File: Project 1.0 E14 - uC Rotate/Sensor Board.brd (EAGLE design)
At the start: 40 x 75.1 mm, 98 parts, among them IC1 LT1963EST-1.5, IC2 LT1963EST-1.5, IC4 LT1963EST-1.5

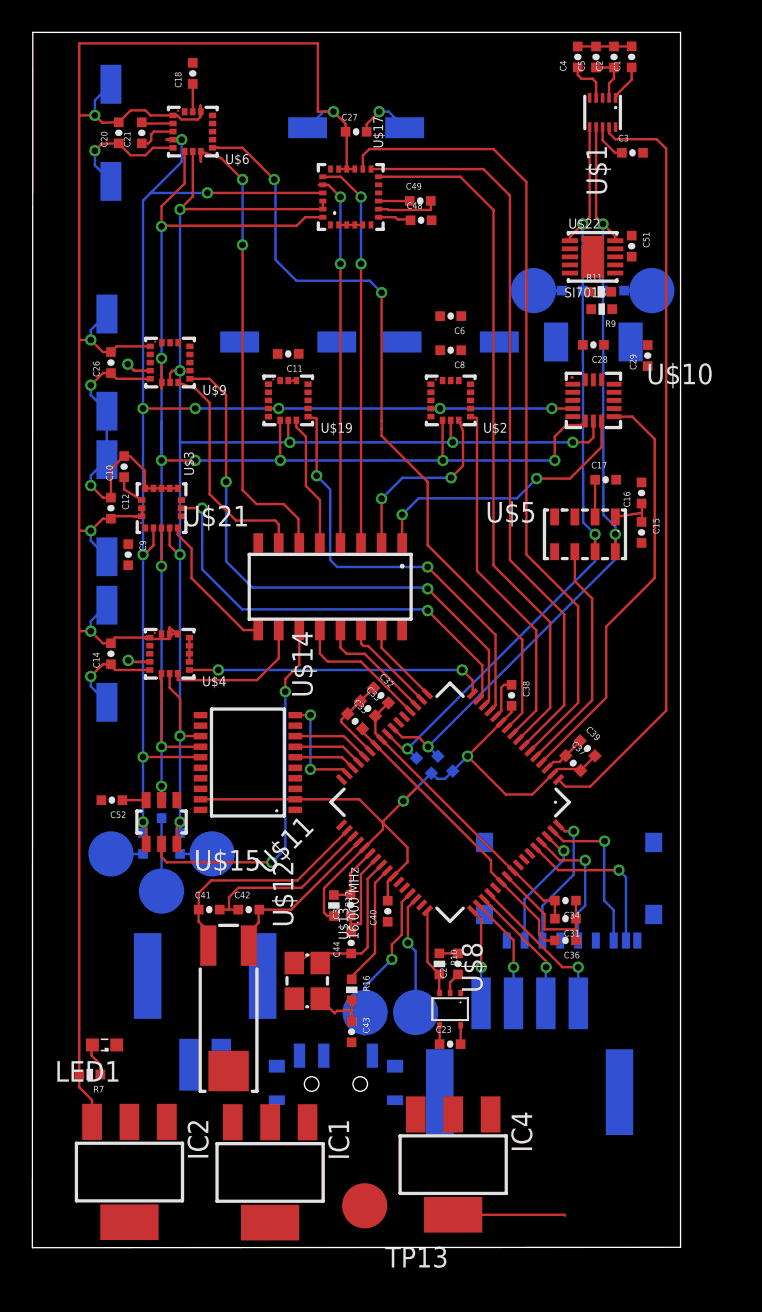
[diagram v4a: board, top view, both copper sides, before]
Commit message: Sensor Test Board: Selected humididty sensor and connected all relevent traces, added two humidity sensors to the libray (Si7005, Si7013). Changed hibernation module crystal to a 2-SMD package and rearanged relevent areas. Added 3 indicator LEDs to pins 57 - 59. Renamed and cleaned up schematic pages (now 7 pages labled by sensor type as apposed to manufacturer. Removed all 3.0V traces and supply and repplaced by 3.3V supply. Most 3.3V traces now routed but waiting for final power consuption calculations before completion. Changed power and programing connectors to smaller profile connectors (1 mm pitch) reducing required space, and cleaned up respective areas. Moved MAG3110 to top of board to for greater seperation from Si7013.
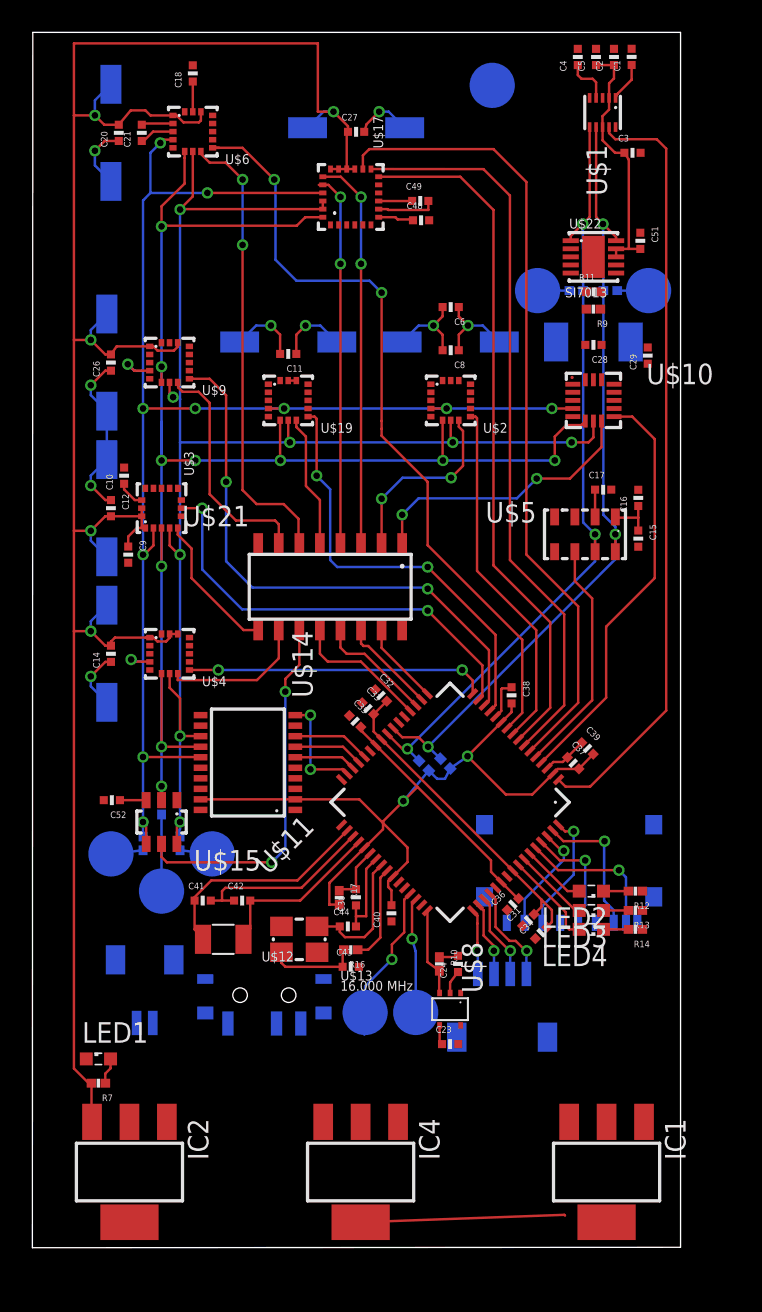
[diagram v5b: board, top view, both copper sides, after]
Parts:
- removed U$16: 5023520200, Kas-Connectors:5023520200
- removed U$20: 5023520410, Kas-Connectors:5023520410
- added J1: 501568-0207, Kas-Connectors:501568-0207
- added LED2, LED3, LED4: Green, eagle-ltspice:LED_SML0603
- added R12, R13, R14: 10k, Kas-Passives:R0402
- added U$7: 501568-0407, Kas-Connectors:501568-0407
- R1, R10, R11, R16, R17, R2, R3, R4, R5, R6, R7, R8, R9: device Kas-Passives:0402-RES -> Kas-Passives:R0402
- U$12: device Kas-Crystal:CYLINDRICAL-(1.9DIAX6L) -> Kas-Crystal:2-SMD(3.2X1.5)
- U$18: device Kas-Connectors:SD-105027-101 -> Kas-Connectors:SD-105027-1001
- moved TP13 69.6 mm to (28.4, 71.7), flipped to the bottom
- moved IC1 20.8 mm to (35.4, 4.62)
- moved S1 7.05 mm to (14.3, 15.5), turned to 0 degrees
- moved IC4 5.73 mm to (20.2, 4.62)
- moved U$12 4.27 mm to (11.8, 19.0), turned to 0 degrees
- moved C43 4.01 mm to (19.6, 17.3), turned to 0 degrees
- moved C36 3.94 mm to (29.6, 21.2), turned to 45 degrees
- moved U$13 2.61 mm to (16.5, 19.0), turned to 0 degrees
- moved C34 2.50 mm to (31.4, 19.4), turned to 45 degrees
- moved R16 2.48 mm to (19.6, 18.4), turned to 180 degrees
- moved C31 2.29 mm to (30.6, 20.2), turned to 45 degrees
- moved U$18 1.09 mm to (33.1, 26.7)
- moved C44 1.04 mm to (19.5, 19.8), turned to 0 degrees
- moved LED1 0.94 mm to (4.05, 11.6), turned to 0 degrees
- moved R7 0.75 mm to (4.05, 10.1)
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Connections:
- removed net N$13: C41.2, C42.1, U$11.P$35
- new net IND-LED-1: LED2.A, U$11.P$59
- new net IND-LED-2: LED3.A, U$11.P$58
- new net IND-LED-3: LED4.A, U$11.P$57
- new net N$29: LED4.C, R14.2
- new net N$31: LED3.C, R13.2
- new net N$35: LED2.C, R12.2
- net 3.0V: no longer R9.2, U$17.P$18, U$2.P$1
- net 3.3V: now also U$17.P$18, U$2.P$1
- net GND: now also C41.2, C42.1, J1.P$1, R12.1, R13.1, R14.1, R9.2, U$11.P$35; no longer U$16.P$1
- net N$19: now also J1.P$2; no longer U$16.P$2
- net SWCLK: now also U$7.P$1; no longer U$20.P$1
- net SWDIO: now also U$7.P$2; no longer U$20.P$2
- net SWO: now also U$7.P$4; no longer U$20.P$4
- net TDI: now also U$7.P$3; no longer U$20.P$3
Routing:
- net 3.3V: track 206.7 -> 228.8 mm, vias 7 -> 9
- net N$13: track 11.1 -> 0.00 mm
- net GND: track 79.3 -> 68.3 mm, vias 5 -> 7
- net IND-LED-3: track 0.00 -> 5.90 mm
- net IND-LED-2: track 0.00 -> 4.71 mm
- net IND-LED-1: track 0.00 -> 4.01 mm
- net SWCLK: track 9.61 -> 6.15 mm
- net SWDIO: track 8.24 -> 5.32 mm
- net TDI: track 7.21 -> 4.66 mm
- net SWO: track 6.31 -> 4.04 mm
- net N$16: track 10.3 -> 8.31 mm
- net N$14: track 3.70 -> 5.62 mm
- net N$17: track 7.63 -> 6.03 mm
- net N$35: track 0.00 -> 1.54 mm
- net N$31: track 0.00 -> 1.54 mm
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
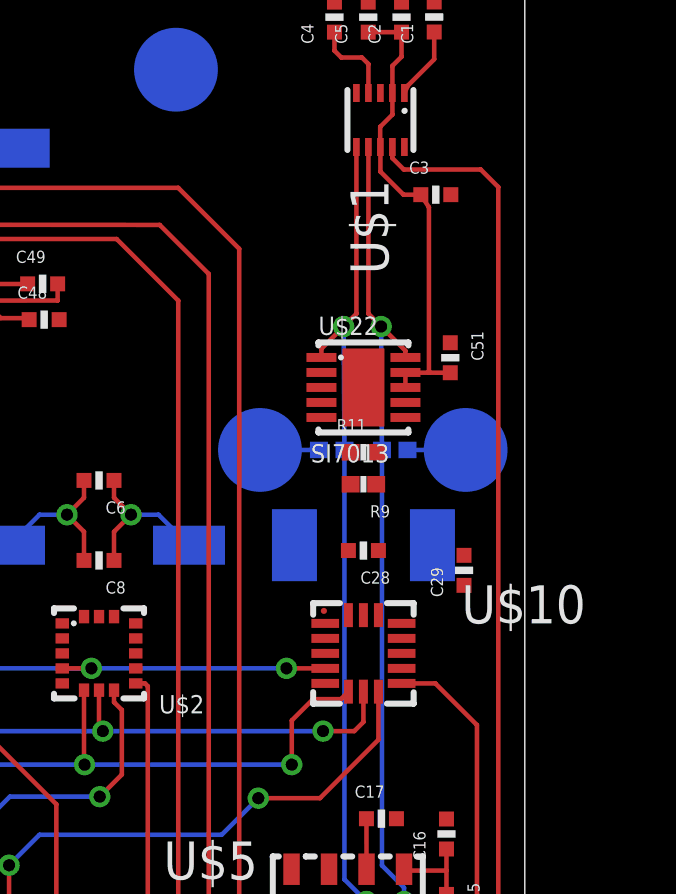
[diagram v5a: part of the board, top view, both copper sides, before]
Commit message: Sensor Test Board: All parts have had their connections reviewed and tickets have been creted were necesery. Componnet footprints that needed checking have been checked and corrected as needed. Any misnamed pads have also been corrected. Missing net names were named and updated.
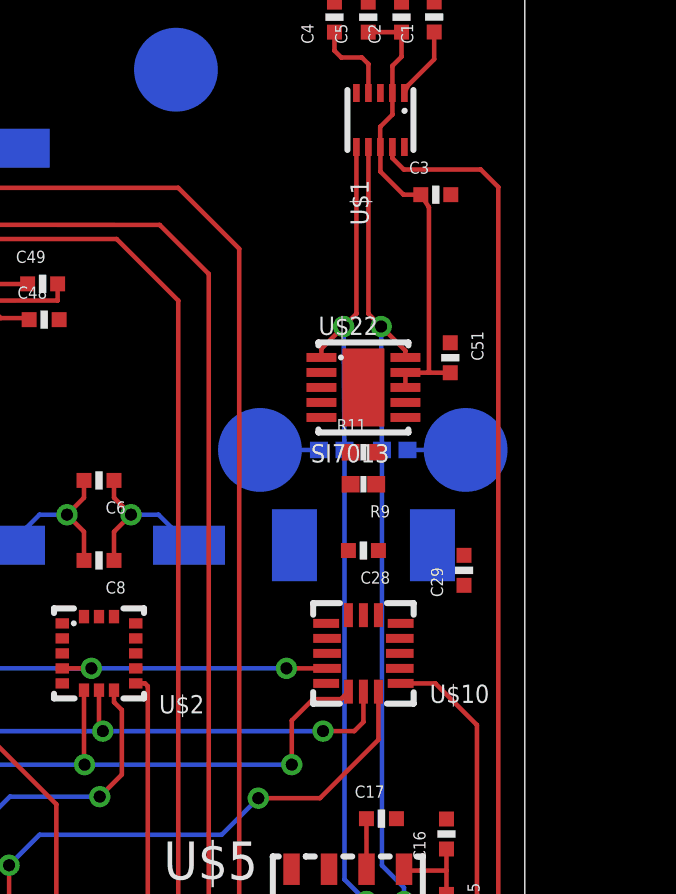
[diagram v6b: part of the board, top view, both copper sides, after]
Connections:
- net CS-ADT7301 renamed !CS-ADT7301
- net CS-ADXL362 renamed !CS-ADXL362
- net CS-H3LIS331DLTR renamed !CS-H3LIS331DLTR
- net CS-LIS3DH renamed !CS-LIS3DH
- net CS-LPS331 renamed !CS-LPS331
- net CS-LS3GD20 renamed !CS-LS3GD20
- net CS-LSM303 renamed !CS-LSM303
- net CS-LSM9D30-G renamed !CS-LSM9D30-G
- net CS-LSM9DS0-XM renamed !CS-LSM9DS0-XM
- net CS-MAX21000 renamed !CS-MAX21000
- removed net 3.0V: IC1.3
- removed net N$2: C52.1, U$15.P$3
- net 3.3V: now also C52.1, U$15.P$3, U$19.P$1, U$2.P$15, U$22.P$5
- net GND: now also U$10.P$5, U$19.P$10, U$2.P$10, U$8.P$1
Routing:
- net 3.3V: track 228.8 -> 230.5 mm
- net N$2: track 1.62 -> 0.00 mm
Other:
- board text added: "Check hibernation pin is connected correctly"

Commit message: Sensor Test Board: Closed tickets 2, 17, 18, 21, 25 and 26. Changed sensor's designations to U from undifined.
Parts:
- renumbered U$1 to U1, U$10 to U10, U$11 to U11, U$14 to U14, U$15 to U15, U$17 to U17, U$18 to J3, U$19 to U19, U$2 to U2, U$21 to U21, U$22 to U22, U$3 to U3, U$4 to U4, U$5 to U5, U$6 to U6, U$7 to U7, U$8 to U8, U$9 to U9
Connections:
- removed net DEN-L3GD: U3.P$8
- net GND: now also U11.P$32, U11.P$43, U11.P$44, U3.P$8
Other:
- board size 40 x 75.1 mm -> 38.5 x 75 mm
- board text added: "Dimensions goal = 38.5x67mm $19.991200372"
- board text removed: "Check hibernation pin is connected correctly"

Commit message: Sensor Test Board: Resolved tickets 23, 20 and 19. The UART connection was moved to PIN 43 and 44 from 45,46 and a connector was added while the test points were moved lower to accomidate the connector.The indicator LEDs were moved from PB4, PB5 and PE4 to PB0 - PB3 with the addition one one more indication LED. The STLM20 was also moved to resolve ticket 19 and is now placed closer to PB4.
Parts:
- added J2: 501568-0207, Kas-Connectors:501568-0207
- added LED5: Green, eagle-ltspice:LED_SML0603
- added R15: 10k, Kas-Passives:R0402
- moved R12 16.8 mm to (21.9, 15.1), turned to 90 degrees
- moved R13 15.2 mm to (23.2, 15.1), turned to 90 degrees
- moved R14 13.6 mm to (24.4, 15.1), turned to 90 degrees
- moved LED2 13.3 mm to (21.9, 17.8), turned to 90 degrees
- moved LED3 11.7 mm to (23.2, 17.8), turned to 90 degrees
- moved LED4 10.3 mm to (24.4, 17.8), turned to 90 degrees
- moved C24 9.80 mm to (35.4, 21.0)
- moved R10 9.80 mm to (34.3, 21.0)
- moved C23 9.80 mm to (34.9, 16.1)
- moved U8 9.80 mm to (34.9, 18.2)
- moved C44 4.04 mm to (15.4, 19.4), turned to 90 degrees
- moved S1 3.77 mm to (13.8, 11.8)
- moved C40 3.11 mm to (19.3, 19.3)
- moved R16 2.97 mm to (16.8, 19.3), turned to 270 degrees
- moved U$13 2.65 mm to (16.2, 16.4), turned to 90 degrees
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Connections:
- removed net U1RX: TP8.P$1, U11.P$45
- removed net U1TX: TP7.P$1, U11.P$46
- new net IND-LED-4: LED5.A, U11.P$48
- new net N$18: LED5.C, R15.2
- new net U6RX: J2.P$1, TP8.P$1, U11.P$43
- new net U6TX: J2.P$2, TP7.P$1, U11.P$44
- net ANALOG-OUT-STLM20: now also U11.P$58; no longer U11.P$48
- net GND: now also R15.1, U17.P$11; no longer R9.2, U11.P$43, U11.P$44
- net IND-LED-1: now also U11.P$45; no longer U11.P$59
- net IND-LED-2: now also U11.P$46; no longer U11.P$58
- net IND-LED-3: now also U11.P$47; no longer U11.P$57
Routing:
- net U1RX: track 9.87 -> 0.00 mm, vias 1 -> 0
- net U6RX: track 0.00 -> 9.53 mm, vias 0 -> 1
- net U6TX: track 0.00 -> 7.99 mm, vias 0 -> 1
- net U1TX: track 7.12 -> 0.00 mm, vias 1 -> 0
- net IND-LED-4: track 0.00 -> 3.06 mm
- net IND-LED-3: track 5.90 -> 2.97 mm
- net GND: track 68.3 -> 70.5 mm
- net N$16: track 8.31 -> 10.2 mm
- net N$10: track 3.64 -> 5.40 mm
- net N$18: track 0.00 -> 1.57 mm
- net IND-LED-2: track 4.71 -> 3.14 mm
- net 3.3V: track 230.5 -> 229.2 mm
- net ANALOG-OUT-STLM20: track 5.46 -> 6.68 mm
- net N$17: track 6.03 -> 6.90 mm
- net !CS-ADT7301: track 22.8 -> 22.1 mm
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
